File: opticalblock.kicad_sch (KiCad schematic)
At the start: 34 parts, among them CN102 Conn_01x12_Socket, IC101 CXA1081, P103 Conn_01x04_Pin, Q101 Q_PNP_Darlington_BCEC

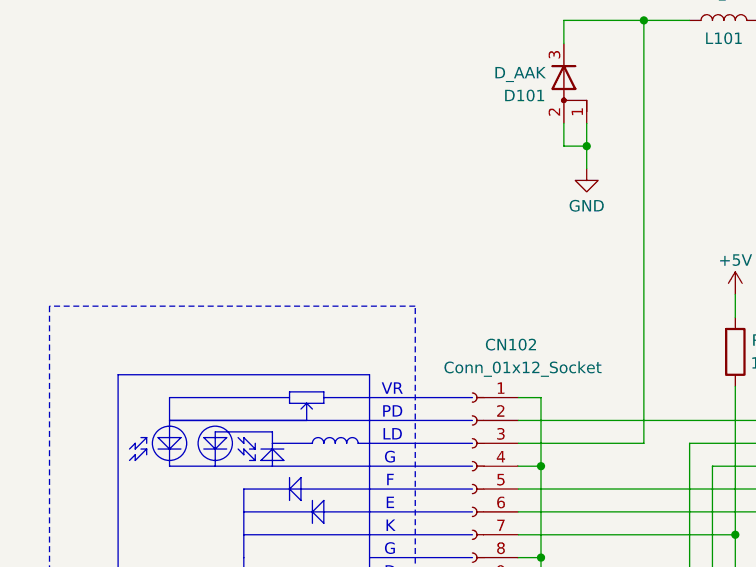
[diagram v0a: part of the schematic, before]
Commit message: Small Schematics update to tidy signals attached to SCSI and MCU chips.
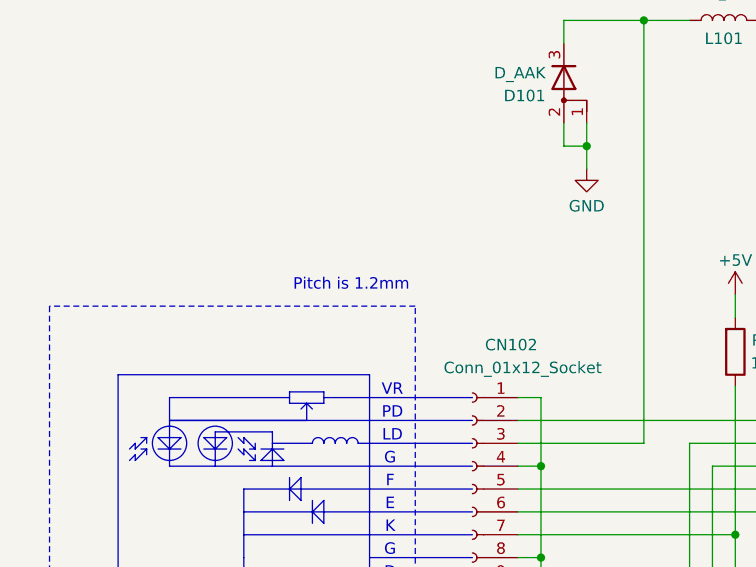
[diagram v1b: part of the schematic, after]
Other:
- note added: "Pitch is 1.2mm"
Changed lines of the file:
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@@
 	(title_block
 		(title "PC-Engine CDR-30A (CD-ROM2) Schematics - MAIN PWR")
-		(date "2024-05-03")
-		(rev "0.1")
+		(date "2024-07-19")
+		(rev "0.2")
 		(company "Author: Regis Galland")
 	)
@@
 		(effects
 			(font
+				(size 1.27 1.27)
+			)
+		)
+	)
+	(text "Pitch is 1.2mm"
+		(exclude_from_sim no)
+		(at 52.578 68.834 0)
+		(effects
+			(font
